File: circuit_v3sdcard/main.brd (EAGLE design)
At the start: 46.9 x 59.4 mm, 21 parts, among them CN1 SD, CN4 5035481020, IC1 C8051F381-GM, IC3 MT29F2G01ABAGDWB, IC4 KC2016K48.0000C1GE00, IC6 MPU-9250

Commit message: Modified circuit
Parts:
- removed CN4: 5035481020, Connector:5035481020
- moved C9 56.5 mm to (19.6, 1.00), turned to 180 degrees
- moved R26 54.1 mm to (19.6, 2.54), turned to 180 degrees
- moved C10 53.9 mm to (19.7, 3.71), turned to 180 degrees
- moved IC3 49.6 mm to (15.3, 5.71), turned to 270 degrees
- moved IC4 49.4 mm to (19.7, 6.30), turned to 90 degrees
- moved IC1 38.1 mm to (16.2, 14.3), turned to 180 degrees
- moved IC6 29.4 mm to (12.4, 19.9), turned to 180 degrees
- moved C1 28.9 mm to (18.8, 18.4), turned to 270 degrees
- moved C6 28.8 mm to (20.0, 18.4), turned to 270 degrees
- moved R2 28.8 mm to (5.36, 18.5), turned to 180 degrees
- moved C4 28.3 mm to (9.86, 23.9), turned to 180 degrees
- moved C3 24.9 mm to (12.0, 23.9), turned to 0 degrees
- moved C2 22.2 mm to (15.4, 21.9), turned to 180 degrees
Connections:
- net C2CK: no longer CN4.9
- net C2D: no longer CN4.10
- net D+: no longer CN4.5
- net D-: no longer CN4.3
- net DGND: now also IC6.B; no longer CN4.7
- net RX1: no longer CN4.4
- net TX1: no longer CN4.2
- net VBUS: no longer CN4.1
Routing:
- net DGND: track 358.5 -> 61.4 mm, vias 19 -> 16
- net +3V3: track 242.3 -> 108.1 mm, vias 10 -> 11
- net N$3: track 104.6 -> 13.0 mm
- net N$6: track 107.3 -> 16.3 mm
- net N$2: track 107.5 -> 19.2 mm
- net N$12: track 103.9 -> 28.8 mm
- net N$10: track 100.0 -> 27.3 mm
- net N$14: track 108.6 -> 39.0 mm
- net D-: track 21.8 -> 57.2 mm, vias 0 -> 2
- net N$11: track 32.1 -> 4.78 mm, vias 2 -> 0
- net D+: track 22.0 -> 44.4 mm, vias 0 -> 2
- net N$4: track 15.3 -> 0.56 mm, vias 2 -> 1
- net C2CK: track 22.4 -> 37.0 mm, vias 4 -> 3
- net EEPROM_MOSI: track 25.2 -> 15.7 mm
- net EEPROM_SCK: track 25.1 -> 15.8 mm
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- added copper zone on layer 16, net DGND
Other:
- board size 46.9 x 59.4 mm -> 47.1 x 59.4 mm

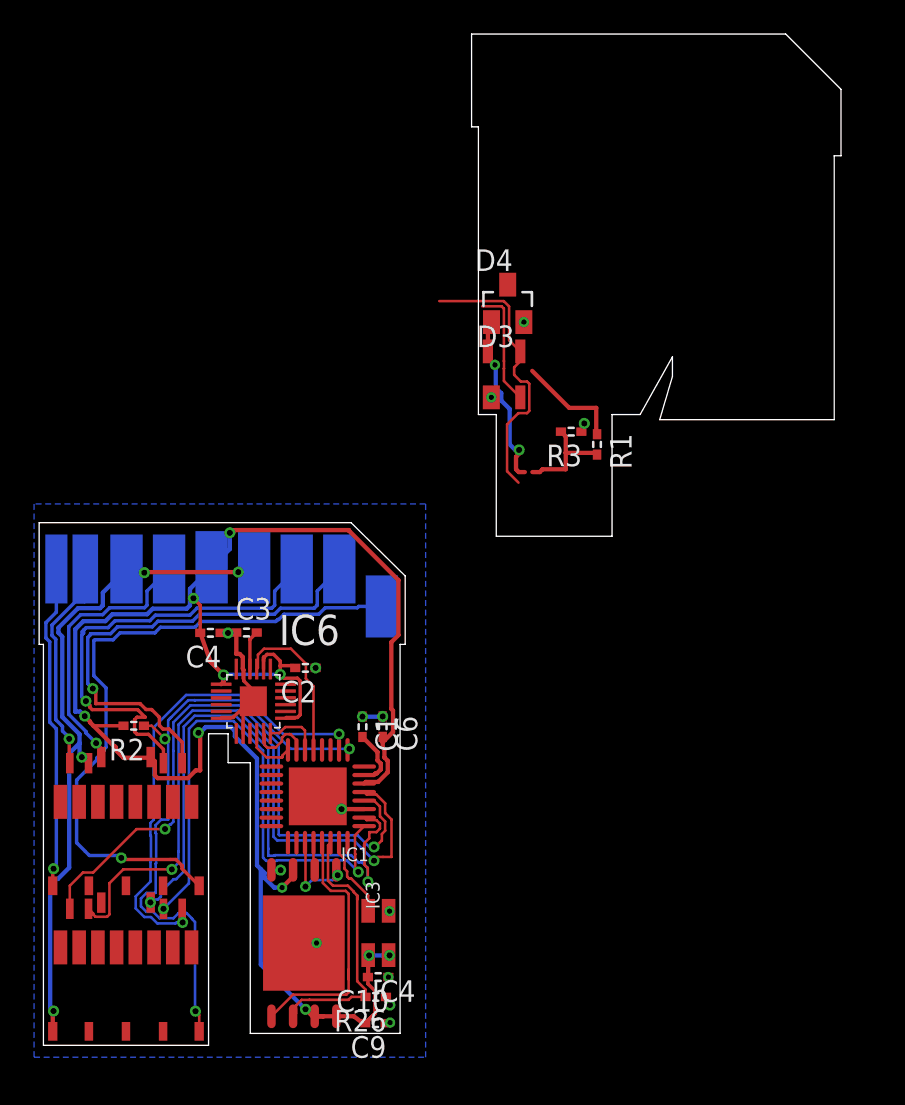
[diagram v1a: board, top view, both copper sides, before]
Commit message: Modified sd circuit
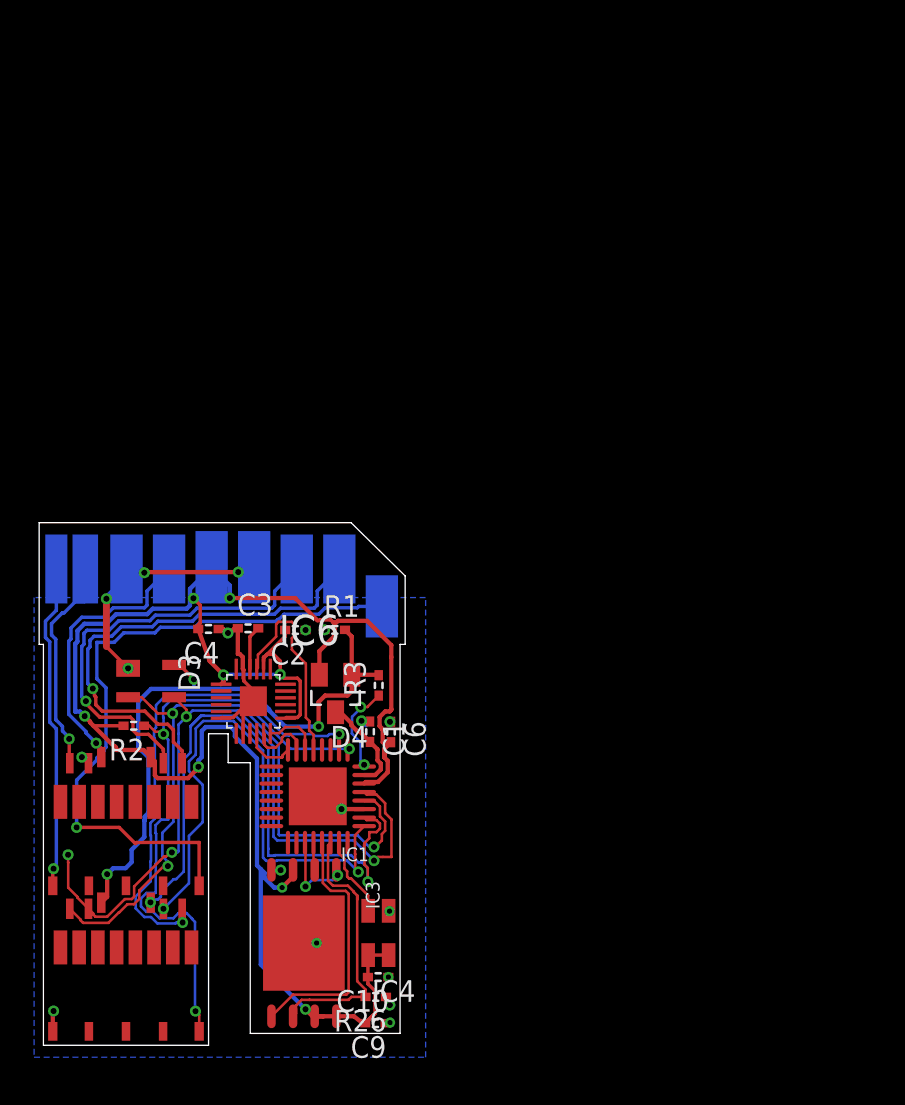
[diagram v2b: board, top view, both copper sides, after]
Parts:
- moved D3 27.5 mm to (6.38, 21.1), turned to 270 degrees
- moved D4 25.0 mm to (17.2, 20.4), turned to 180 degrees
- moved R1 18.9 mm to (17.2, 24.1), turned to 0 degrees
- moved R3 18.7 mm to (19.7, 20.8), turned to 90 degrees
- moved C2 2.30 mm to (14.8, 24.1)
- moved C6 0.58 mm to (20.5, 18.1)
- moved C1 0.53 mm to (19.2, 18.1)
- moved C3 0.27 mm to (12.1, 24.2)
- moved C4 0.25 mm to (9.74, 24.2)
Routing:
- net DGND: track 61.4 -> 33.6 mm, vias 16 -> 18
- net VBUS: track 16.5 -> 36.6 mm, vias 2 -> 3
- net D-: track 57.2 -> 44.5 mm, vias 2 -> 4
- net N$4: track 0.56 -> 5.34 mm, vias 1 -> 2
- net N$1: track 2.90 -> 5.81 mm
- net IMU_MISO: track 9.45 -> 12.3 mm
- net N$10: track 27.3 -> 25.7 mm
- net D+: track 44.4 -> 43.3 mm, vias 2 -> 3
- net +3V3: track 108.1 -> 109.1 mm, vias 11 -> 8
- net C2D: track 28.6 -> 29.5 mm
- net TX1: track 36.4 -> 37.3 mm
- net EEPROM_MOSI: track 15.7 -> 15.1 mm
- net N$12: track 28.8 -> 28.2 mm
- net N$14: track 39.0 -> 39.6 mm
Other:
- board size 47.1 x 59.4 mm -> 21.5 x 30.7 mm

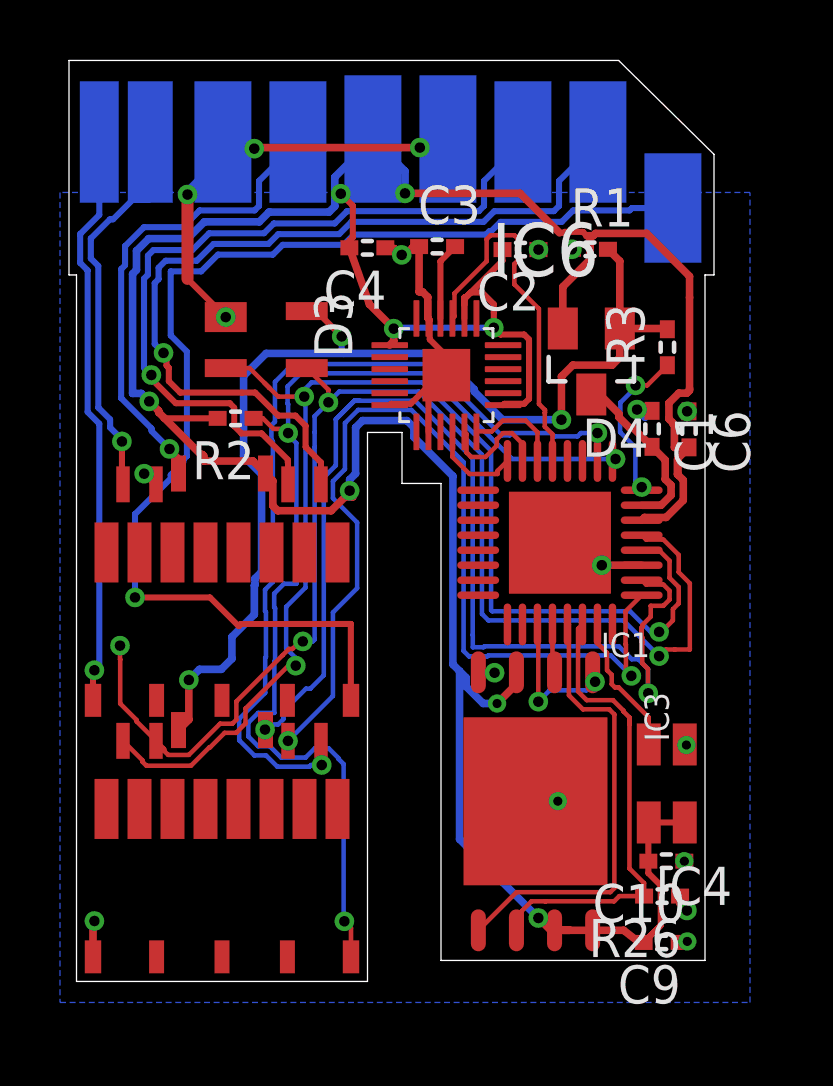
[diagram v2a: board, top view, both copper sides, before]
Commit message: Modified circuit to generate garber file
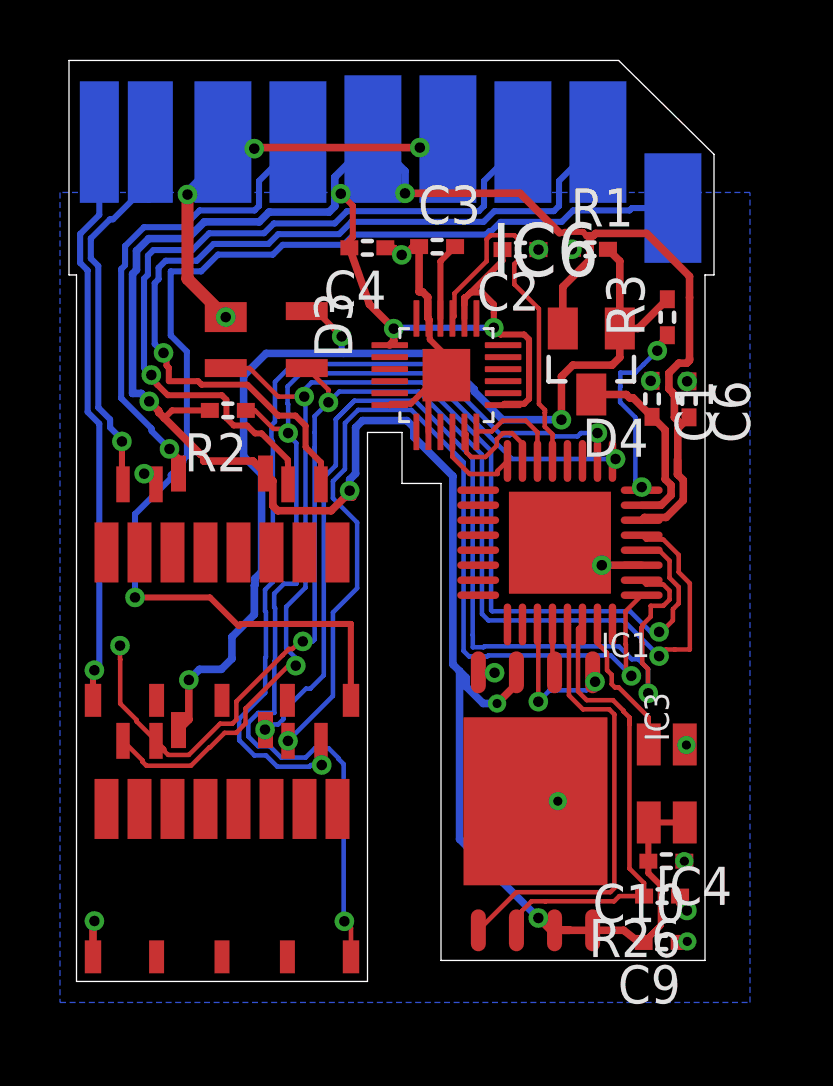
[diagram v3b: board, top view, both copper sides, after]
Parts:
- moved C1 1.00 mm to (19.2, 19.1)
- moved C6 1.00 mm to (20.5, 19.1)
- moved R3 1.00 mm to (19.7, 21.8)
- moved R2 0.37 mm to (5.09, 18.7)
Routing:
- net DGND: track 33.6 -> 32.3 mm
- net N$4: track 5.34 -> 6.41 mm
- net N$1: track 5.81 -> 6.33 mm
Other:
- board text added: "virtualGimbal rev.4.1"
- board text removed: "virtualGimbal v3"
